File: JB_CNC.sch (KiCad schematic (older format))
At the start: 80 parts, among them CON1 POWER_IN, J1 Arduino_Header, P1 Z_CTRL, P10 X_LIMIT_1, P11 Y_LIMIT_1, P12 Z_LIMIT_1, P13 FLUIDO, P14 X_LIMIT_2, P15 Y_LIMIT_2, P16 Z_LIMIT_2, P17 SPINDLE_PWR, P18 SPINDLE_LED_ON, P19 SPINDLE_DIRECTION, P2 Z_LIMIT, P20 RESET/ABORT, P21 START/RESUME, P22 FEED_HOLD, P23 SAFETY_DOOR, P24 ASPIRADOR, P25 earth, P26 SPINDLE_LED_OFF, P3 Y_CTRL, P4 Y_LIMIT, P5 X_CTRL, P6 X_LIMIT, P7 USB_TO_ARDUINO, P8 F_INV, P9 USB_SHIELD_INPUT, Q1 BC546, Q2 BC546, Q3 BC546, Q4 BC546, Q5 BC546, U1 CA3140, U2 LM7805CT, U3 CA3140, U4 74LS86, u657 1N4001

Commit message: Circuito Redesenhado
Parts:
- removed 1N2, DFDSF1, u657: 1N4001, Diodes_ThroughHole:Diode_DO-35_SOD27_Horizontal_RM10, symbol D
- removed CON1: POWER_IN, Connect:BARREL_JACK, symbol BARREL_JACK
- removed P17: SPINDLE_PWR, w_conn_kk100:kk100_22-23-2021, symbol CONN_01X02
- removed P19: SPINDLE_DIRECTION, w_conn_kk100:kk100_22-23-2021, symbol CONN_01X02
- removed Q3: BC546, TO_SOT_Packages_THT:TO-92_Inline_Wide, symbol BC546
- removed R17, R19: 2k7, Resistors_ThroughHole:Resistor_Horizontal_RM10mm, symbol R
- removed R25: 10k, Resistors_ThroughHole:Resistor_Horizontal_RM10mm, symbol R
- removed TRIMM1: 10k, symbol POT-RESCUE-JB_CNC_0.9
- removed U4: 74LS86, Housings_DIP:DIP-14_W7.62mm_LongPads, symbol 74LS86
- added 1N1: 1N4001, Diodes_ThroughHole:Diode_DO-35_SOD27_Horizontal_RM10, symbol D
- added C10: 1uF, Capacitors_ThroughHole:C_Radial_D5_L11_P2.5, symbol CP
- added D3: 1K5E68A, Diodes_ThroughHole:Diode_P600_Vertical_KathodeUp, symbol D_TVS
- added P13: ASPIRADOR, w_conn_kk100:kk100_22-23-2021, symbol CONN_01X02
- added P17: SPINDLE_PWR, w_conn_kk100:kk100_22-23-2031, symbol CONN_01X03
- added P26: DIREÇÃO, w_conn_kk100:kk100_22-23-2041, symbol CONN_01X04
- added Q1: BC546, TO_SOT_Packages_THT:TO-92_Inline_Wide, symbol BC546
- added R15: 470, Resistors_ThroughHole:Resistor_Vertical_RM5mm, symbol R-RESCUE-JB_CNC
- added R16, R7: 68k, Resistors_ThroughHole:Resistor_Vertical_RM5mm, symbol R-RESCUE-JB_CNC
- added R22, R33, R34, R36, R6: 1k, Resistors_ThroughHole:Resistor_Vertical_RM5mm, symbol R-RESCUE-JB_CNC
- added R23, R27, R29: 10k, Resistors_ThroughHole:Resistor_Vertical_RM5mm, symbol R-RESCUE-JB_CNC
- added R28, R35, R37: 4k7, Resistors_ThroughHole:Resistor_Vertical_RM5mm, symbol R-RESCUE-JB_CNC
- added R3: 22k, Resistors_ThroughHole:Resistor_Vertical_RM5mm, symbol R-RESCUE-JB_CNC
- added R5: 2k7, Resistors_ThroughHole:Resistor_Vertical_RM5mm, symbol R-RESCUE-JB_CNC
- added U10: 74LS32, Housings_DIP:DIP-14_W7.62mm_LongPads, symbol 74LS32
- added U3, U5, U6: 4N25, Housings_DIP:DIP-6_W7.62mm_LongPads, symbol 4N25
- added W1: FONTE, Connect:bornier2, symbol BORNIER
- C1: value 470nF -> 1uF
- C11: renamed from C10; footprint (none) -> Capacitors_ThroughHole:C_Radial_D5_L11_P2.5; symbol C -> CP
- C12: renamed from C2; footprint Capacitors_ThroughHole:C_Radial_D5_L11_P2.5 -> Capacitors_ThroughHole:C_Radial_D10_L13_P5
- C13: renamed from C3; footprint Capacitors_ThroughHole:C_Radial_D5_L11_P2.5 -> Capacitors_ThroughHole:C_Radial_D6.3_L11.2_P2.5
- C2: renamed from C4; footprint (none) -> Capacitors_ThroughHole:C_Radial_D5_L11_P2.5; symbol C -> CP
- C3: renamed from C5; footprint (none) -> Capacitors_ThroughHole:C_Radial_D5_L11_P2.5; symbol C -> CP
- C4: renamed from C6; footprint (none) -> Capacitors_ThroughHole:C_Radial_D5_L11_P2.5; symbol C -> CP
- C5: renamed from C7; footprint (none) -> Capacitors_ThroughHole:C_Radial_D5_L11_P2.5; symbol C -> CP
- C6: renamed from C8; footprint (none) -> Capacitors_ThroughHole:C_Radial_D5_L11_P2.5; symbol C -> CP
- C7: renamed from C9; footprint (none) -> Capacitors_ThroughHole:C_Radial_D5_L11_P2.5; symbol C -> CP
- C8: renamed from C11; footprint (none) -> Capacitors_ThroughHole:C_Radial_D5_L11_P2.5; symbol C -> CP
- C9: renamed from C12; footprint (none) -> Capacitors_ThroughHole:C_Radial_D5_L11_P2.5; symbol C -> CP
- D1: footprint (none) -> Diodes_ThroughHole:Diode_P600_Vertical_KathodeUp
- D2: value LED -> LED_PWR
- J1: footprint cta_arduinos:arduino_uno_header -> w_conn_misc:arduino_header
- P19: renamed from P20; value RESET/ABORT -> RESETA/INTERROMPE
- P20: renamed from P21; value START/RESUME -> INICIA/CONTINUA
- P21: renamed from P22; value FEED_HOLD -> PAUSA
- P22: renamed from P24; value ASPIRADOR -> SONDA
- P23: value SAFETY_DOOR -> PORTA_SEGURANÇA
- P24: renamed from P25; footprint Socket_Strips:Socket_Strip_Straight_1x01 -> w_details:hole_1mm
- P25: renamed from P26; value SPINDLE_LED_OFF -> SPINDLE_LED_ON; footprint (none) -> w_conn_kk100:kk100_22-23-2021
- P27: renamed from P18; value SPINDLE_LED_ON -> SPINDLE_LED_OFF
- P7: value USB_TO_ARDUINO -> USB_PARA_ARDUINO; footprint Connect:USB_A -> w_conn_pc:conn_usb_A; symbol USB_A-RESCUE-JB_CNC -> USB_A-RESCUE-JB_CNC_0.9
- P9: value USB_SHIELD_INPUT -> ENTRADA_USB_SHIELD; footprint Connect:USB_B -> w_conn_pc:conn_usb_B; symbol USB_B-RESCUE-JB_CNC -> USB_B-RESCUE-JB_CNC_0.9
- Q5: symbol BC817-40 -> BC546
- R1: value 100k -> 10k; footprint Resistors_ThroughHole:Resistor_Horizontal_RM10mm -> Resistors_ThroughHole:Resistor_Vertical_RM5mm; symbol R -> R-RESCUE-JB_CNC
- R10: renamed from R7; value 22k -> 10k; footprint (none) -> Resistors_ThroughHole:Resistor_Vertical_RM5mm; symbol R -> R-RESCUE-JB_CNC
- R11: renamed from R8; value 22k -> 10k; footprint (none) -> Resistors_ThroughHole:Resistor_Vertical_RM5mm; symbol R -> R-RESCUE-JB_CNC
- R12: renamed from R9; value 22k -> 10k; footprint (none) -> Resistors_ThroughHole:Resistor_Vertical_RM5mm; symbol R -> R-RESCUE-JB_CNC
- R13: renamed from R10; value 22k -> 10k; footprint (none) -> Resistors_ThroughHole:Resistor_Vertical_RM5mm; symbol R -> R-RESCUE-JB_CNC
- R14: renamed from R15; value 1k -> 10k; footprint Resistors_ThroughHole:Resistor_Horizontal_RM10mm -> Resistors_ThroughHole:Resistor_Vertical_RM5mm; symbol R -> R-RESCUE-JB_CNC
- R17: renamed from R5; footprint Resistors_ThroughHole:Resistor_Horizontal_RM10mm -> Resistors_ThroughHole:Resistor_Vertical_RM5mm; symbol R -> R-RESCUE-JB_CNC
- R18: renamed from R12; value 22k -> 1k; footprint (none) -> Resistors_ThroughHole:Resistor_Vertical_RM5mm; symbol R -> R-RESCUE-JB_CNC
- R19: renamed from R13; value 22k -> 1k; footprint (none) -> Resistors_ThroughHole:Resistor_Vertical_RM5mm; symbol R -> R-RESCUE-JB_CNC
- R2: value 6k2 -> 20k; footprint Resistors_ThroughHole:Resistor_Horizontal_RM10mm -> Resistors_ThroughHole:Resistor_Vertical_RM5mm; symbol R -> R-RESCUE-JB_CNC
- R20: renamed from R21; value 22k -> 10k; footprint Resistors_ThroughHole:Resistor_Horizontal_RM10mm -> Resistors_ThroughHole:Resistor_Vertical_RM5mm; symbol R -> R-RESCUE-JB_CNC
- R21: renamed from R14; value 22k -> 10k; footprint Resistors_ThroughHole:Resistor_Horizontal_RM10mm -> Resistors_ThroughHole:Resistor_Vertical_RM5mm; symbol R -> R-RESCUE-JB_CNC
- R24: renamed from R16; value 22k -> 1k; footprint (none) -> Resistors_ThroughHole:Resistor_Vertical_RM5mm; symbol R -> R-RESCUE-JB_CNC
- R25: renamed from R23; value 22k -> 10k; footprint Resistors_ThroughHole:Resistor_Horizontal_RM10mm -> Resistors_ThroughHole:Resistor_Vertical_RM5mm; symbol R -> R-RESCUE-JB_CNC
- R26: renamed from R24; footprint Resistors_ThroughHole:Resistor_Horizontal_RM10mm -> Resistors_ThroughHole:Resistor_Vertical_RM5mm; symbol R -> R-RESCUE-JB_CNC
- R30: renamed from R11; value 10k -> 4k7; footprint (none) -> Resistors_ThroughHole:Resistor_Vertical_RM5mm; symbol R -> R-RESCUE-JB_CNC
- R31: renamed from R26; value 2k2 -> 1k; footprint Resistors_ThroughHole:Resistor_Horizontal_RM10mm -> Resistors_ThroughHole:Resistor_Vertical_RM5mm; symbol R -> R-RESCUE-JB_CNC
- R32: renamed from R27; value 10k -> 4k7; footprint Resistors_ThroughHole:Resistor_Horizontal_RM10mm -> Resistors_ThroughHole:Resistor_Vertical_RM5mm; symbol R -> R-RESCUE-JB_CNC
- R4: footprint Resistors_ThroughHole:Resistor_Horizontal_RM10mm -> Resistors_ThroughHole:Resistor_Vertical_RM5mm; symbol R -> R-RESCUE-JB_CNC
- R8: renamed from R3; value 22k -> 10k; footprint (none) -> Resistors_ThroughHole:Resistor_Vertical_RM5mm; symbol R -> R-RESCUE-JB_CNC
- R9: renamed from R6; value 22k -> 10k; footprint (none) -> Resistors_ThroughHole:Resistor_Vertical_RM5mm; symbol R -> R-RESCUE-JB_CNC
- U2: renamed from U3; footprint (none) -> Housings_DIP:DIP-8_W7.62mm_LongPads
- renumbered 1N1 to 1N3, P13 to P18, Q1 to Q3, U2 to U4
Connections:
- net labels added: +24V(EXT), CCW/STOP, CW/STOP, FEED_HOLD*, GND(EXT), GNDPWR, LIG/DESL, PROBE*, RESET/ABORT*, START/RESUME*, VCC, X_LIMIT*, X_LIMIT_A, X_LIMIT_B, Y_LIMIT*, Y_LIMIT_A, Y_LIMIT_B, Z_LIMIT*, Z_LIMIT_A, Z_LIMIT_B
- net labels removed: +14V, Earth, FEED_HOLD, PROBE, RESET/ABORT, START/RESUME, X_LIMIT, X_LIMIT_1, X_LIMIT_2, Y_LIMIT, Y_LIMIT_1, Y_LIMIT_2, Z_LIMIT, Z_LIMIT_1, Z_LIMIT_2
- wire segments 208 -> 247
- no-connect marks 15 -> 14
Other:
- note added: "Amplificação do sinal SPINDLE_DIR para utilização no \ninversor de frequência:\n\nO Inversor dispõe de duas entradas de controle de \ndireção: HORARIO/PARADO(CW/STOP) e \nANTIHORÁRIO/PARADO (CCW/STOP), que no caso de uma\nestar ativada (HIGH), a outra deve estar desativada.\nPara acionar uma ou a outra, utiliza-se um circuito \ntransistorizado com optoisoladores para controlar esses\nsinais e iso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"
- note added: "Ativação do aspirador de acordo com spindle \n\nO aspirador deve sempre estar ligado enquanto\no spindle estiver em operação. Para isto, usa-se \num circuito transistorizado identico ao do spindle\nque ativa/desativa o relé do aspirador exatamente \nquando o relé de ativação do spindle for \nativado/desativado.\nDevido a altas correntes, foi colocado somente\no pino, pois o relé e o circuito de a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"
- note added: "Ativação/Desativação do spindle + aspirador via PWM:\n\nComo nessa versão do GRBL temos o pino SPINDLE_PWM\nsubstituindo o pino SPINDLE_EN, o spindle é ativado\ndiretamente no PWM do arduíno via GRBL. Como o valor V_CTRL\nnunca chega totalmente a zero, o spindle nunca pára.\nPara resolver esse problema, usa-se um circuito transistorizado\nque dá nível lógico zero na entrada de controle de ativaçã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"
- note added: "Circuito conversor Analog-Digital + Amplificador.\n\nComo o inversor de frequência utilizado trabalha \nsomente com valores analógicos de tensão, o sinal\ndo PWM é convertido para o valor equivalente de \ntensão analógica e amplificado para escala máxima\nde 0-10V de modo que o inversor de frequência \nreconheça o valor de velocidade que o GRBL solicita ."
- note added: "Fins de curso mecânicos. \nNormalmente fechados. Pulldown externo.\nPinos 1 e 2 podem ser NF ou NA,\ndependendo das lógica digital usada.\nDebounce: 15ms"
- note added: "Fonte: 14.8 - 15VDC VCC: 14.1 - 14.4V\nDiodo Ultra Rápido para Polarização Reversa.\nDiodo TVS para surtos de tensão\nRegulador de Tensão para 5V.\n"
- note added: "Logica digital de fim de curso:\nO arduíno detecta fim de curso\nsem diferenciar se o fim de curso\né máximo ou mínimo.\nOs drivers dos motores de passo \ndiferenciam isso, portanto sugere-se\nutilizar portas lógicas para isolar \no arduíno dos motores de passo\npara que ambos possam receber \ncomandos dos sensores de fim de \ncurso sem afetar um ao outro.\nObs.: Para lógica inversa\n(0 para HIGH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"
- note added: "Os botões de comando do GRBL usam\npullup interno por padrão, ou seja, \nATIVO-BAIXO com chave NA.\nUsam-se pulldown com filtros para \ndebouncing (15ms) e uma chave NF\npara manter o ACTIVE LOW.\n"
- note added: "Pino para e desativar o relé de alimentação\nda bomba de fluído arrefecedor.\n\nDevido a altas correntes, foi colocado somente\no pino, pois o relé e o circuito de alimentação \nda bomba serão colocados numa placa separada."
- note added: "Pino para entrada da sonda de contato\n(Referência variável para o eixo Z)\nPulldown com filtros para \ndebouncing (15ms).\n"
- note added: "Sensor da porta \nPino 1 NF\nPino 2 NA\nPino 3 Conn\nDebounce: 15ms\n"
- note added: "Sinalizador de segurança SPINDLE_LED.\n\nQuando o spindle é ligado, o LED_SPINDLE_ON \n(LED vermelho externo) é ativado, sinalizando\nque não é seguro mexer na máquina, pois o \nspindle está ligado, ou seja, a máquina está\nem operação. Quando o spindle é desligado,\nentão LED_SPINDLE_OFF (LED verde externo) é\nativado, sinalizando que é seguro mexer \nna máquina."
- note removed: "Amplificação do sinal SPINDLE_DIR para\nutilizar no inversor de frequência:\n\nO relé de ativação das entradas do inversor\nde frequência é do tipo 12V, portanto usa-se\num circuito transistorizado para amplificar o\nsinal do arduíno de 5 para 14V com corrente\nsuficiente para ativar o relé.\n"
- note removed: "Ativação e desativação do spindle via PWM:\n\nComo nessa versão do GRBL temos o pino\nSPINDLE_PWM substituindo o pino SPINDLE_EN,\no spindle é ativado diretamente no PWM do arduíno\nvia GRBL.\nComo o valor V_CTRL nunca chega totalmente a zero, \no spindle nunca pára.\nPara resolver esse problema, sugere-se um circuito\ntransistorizado que dá nível lógico zero na entrada de \ncontrole de ativação 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"
- note removed: "Circuito conversor Analog-Digital + Amplificador.\n\nComo o inversor de frequência utilizado trabalha \nsomente com valores analógicos de tensão, o sinal\ndo PWM é convertido para o valor equivalente de \ntensão analógica e amplificado numa escala máxima\nde 1:2.61 para trimmer setado no seu valor maximo (10k)\nde modo que o inversor de frequência reconheça\no valor de velocidade que o GRBL solic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"
- note removed: "Diodo Ultra Rápido para Polarização Reversa.\nRegulador de Tensão para 5V."
- note removed: "Fins de curso mecânicos. \nNormalmente fechados. Pulldown externo.\nPino 1 NF. Pino 2 NA. Pino 3 Conn.\nDebounce: 20ms"
- note removed: "Logica digital de fim de curso:\nO arduíno detecta fim de curso\nsem diferenciar se o fim de curso\né máximo ou mínimo.\nOs drivers dos motores de passo \ndiferenciam isso, portanto sugere-se\nutilizar portas lógicas para isolar \no arduíno dos motores de passo\npara que ambos possam receber \ncomandos dos sensores de fim de \ncurso sem afetar um ao outro.\nObs.: Para níveis lógicos invertidos\n(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"
- note removed: "Os botões de comando do GRBL usam\npullup interno por padrão, ou seja, \nACTIVE LOW com chave NA.\nUsarão-se pulldown com filtros para \ndebouncing (20ms) e uma chave NF\npara manter o ACTIVE LOW.\n"
- note removed: "Pino para ativar e desativar o relé de alimentação\ndo aspirador\n\nDa mesma forma que foi feito na bomba de fluído \narrefecedor, deixa-se somente o pino para ativar e\ndesativar o relé de alimentação.\n"
- note removed: "Pino para e desativar o relé de alimentação\nda bomba de fluído arrefecedor.\n\nDevido a altas correntes, foi colocado somente\no pino, pois o relé de alimentação da bomba \nserá colocado numa placa separada."
- note removed: "Sensor da porta \nPino 1 NF\nPino 2 NA\nPino 3 Conn\nDebounce: 20ms\n"
- note removed: "Sinalizador de segurança SPINDLE_LED.\n\nQuando o spindle é ligado, o led_spindle_on \n(LED vermelho externo) é ativado, sinalizando\nque não é seguro mexer na máquina, pois o \nspindle está ligado, ou seja, a máquina está\nem operação. Quando o spindle é desligado,\nentão led_spindle_off (LED verde externo) é\nativado, sinalizando que é seguro mexer \nna máquina."
- moved on the sheet: U1

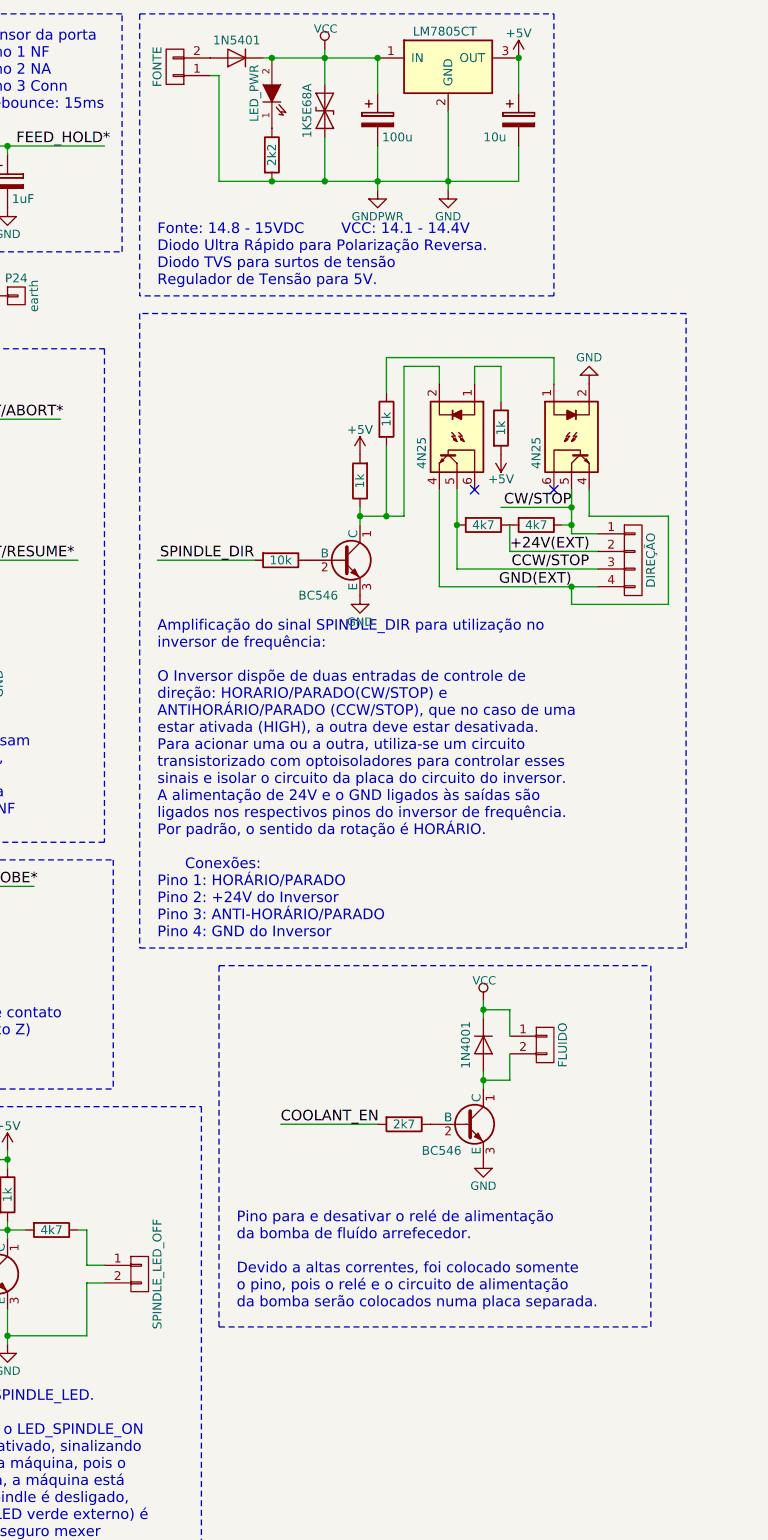
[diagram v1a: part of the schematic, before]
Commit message: Adicionado Fusível
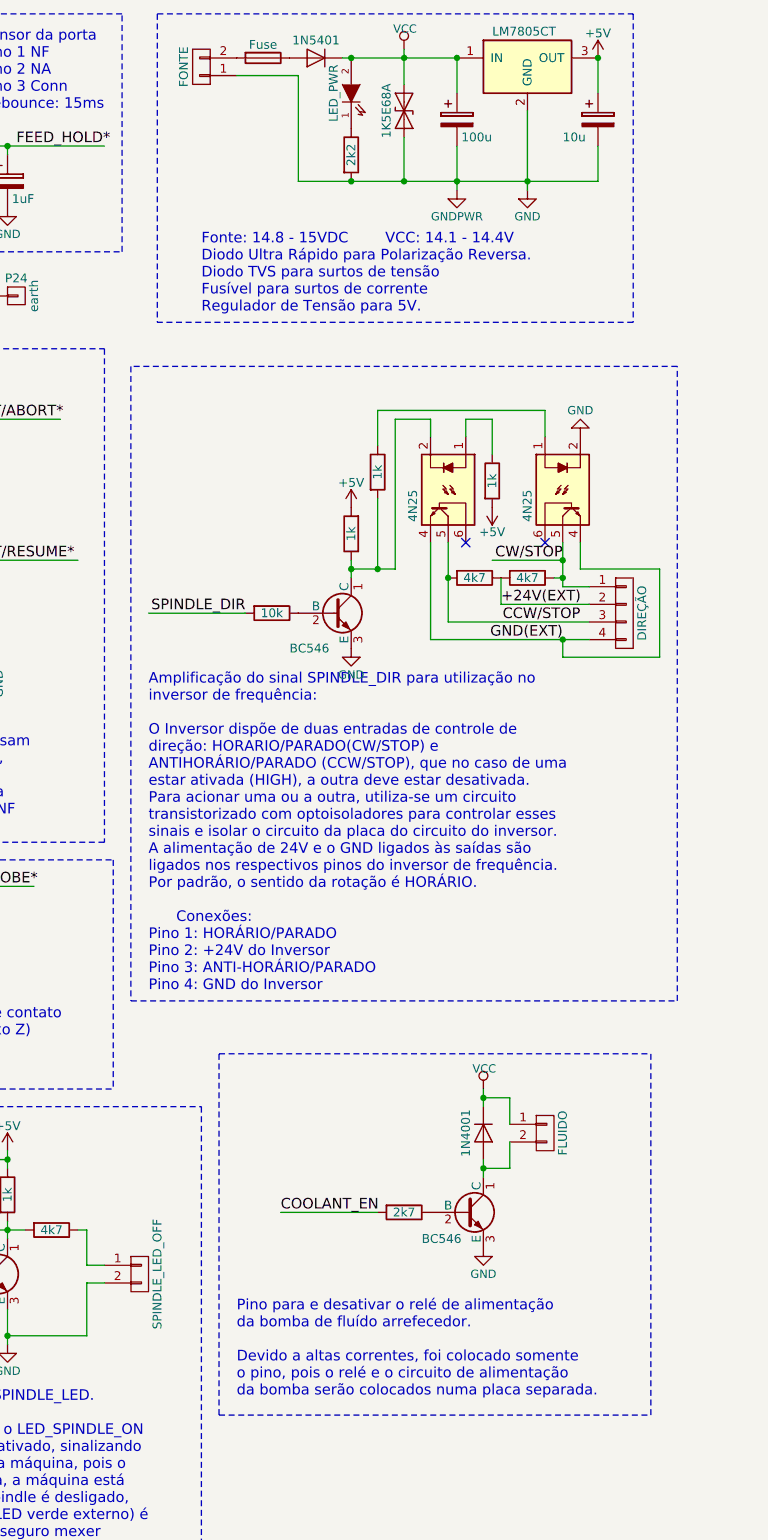
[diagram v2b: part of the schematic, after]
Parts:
- added F1: Fuse, w_misc_comp:fuse_holder_CQ-2, symbol Fuse
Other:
- note added: "Fonte: 14.8 - 15VDC VCC: 14.1 - 14.4V\nDiodo Ultra Rápido para Polarização Reversa.\nDiodo TVS para surtos de tensão\nFusível para surtos de corrente\nRegulador de Tensão para 5V."
- note removed: "Fonte: 14.8 - 15VDC VCC: 14.1 - 14.4V\nDiodo Ultra Rápido para Polarização Reversa.\nDiodo TVS para surtos de tensão\nRegulador de Tensão para 5V.\n"
